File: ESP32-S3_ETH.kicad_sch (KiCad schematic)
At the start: 14 parts, among them J1 Screw_Terminal_01x02, J2 Screw_Terminal_01x04, J3 SSW-104-01-F-S, J4 SSW-108-02-G-D, J5 Screw_Terminal_01x03, J6 Screw_Terminal_01x03, U1 ESP32-S3-ETH

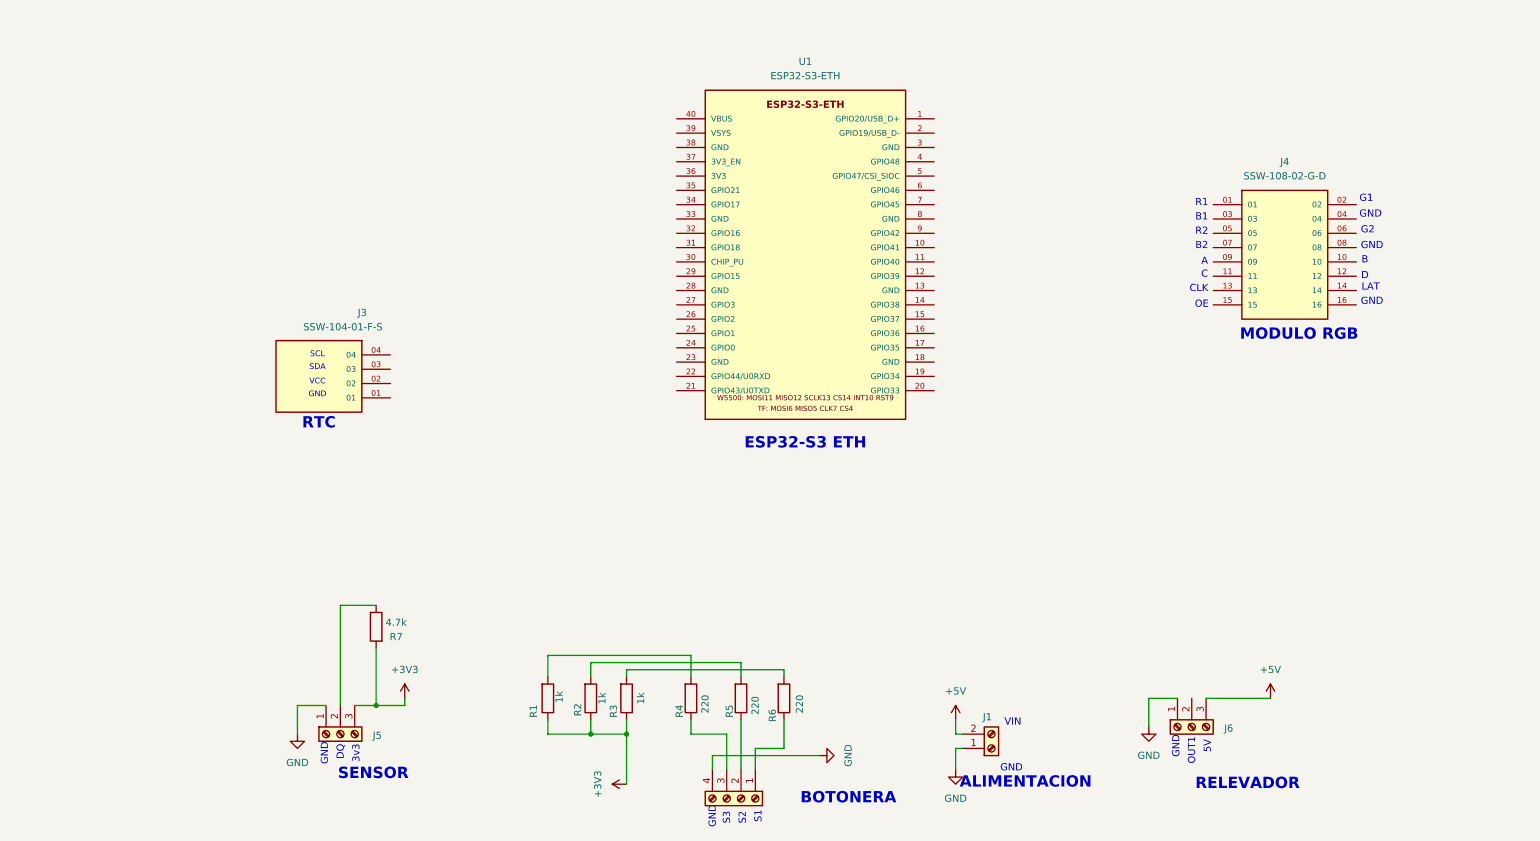
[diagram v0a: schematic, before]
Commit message: ssw-120-1 added
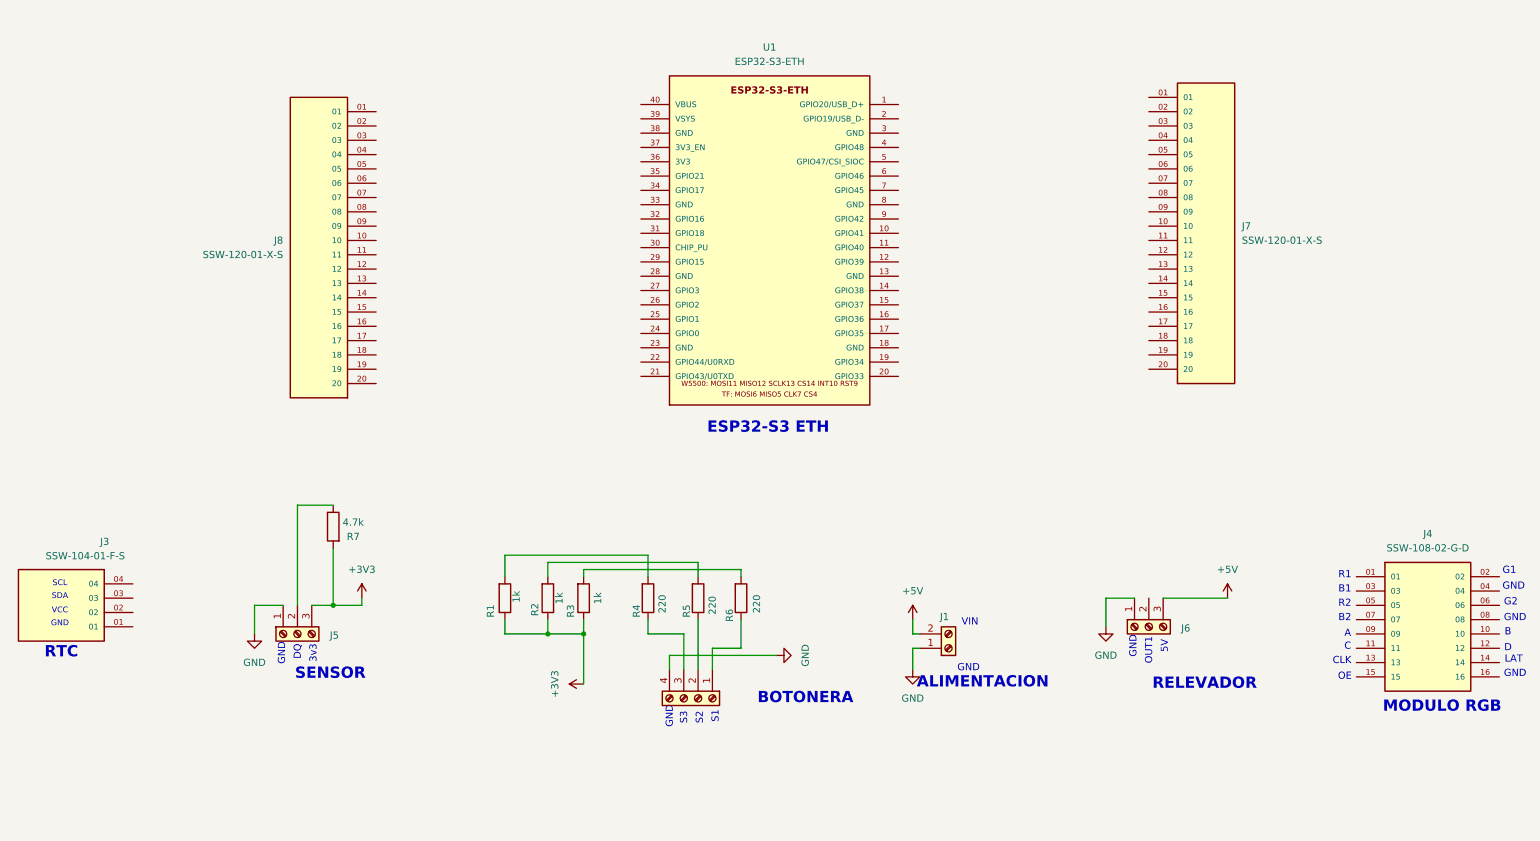
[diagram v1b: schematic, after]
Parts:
- added J7, J8: SSW-120-01-X-S, symbol SSW-120-01-X-S:SSW-120-01-X-S
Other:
- moved on the sheet: J1, J3, J4, J5, J6, R1, R2, R3, R4, R5, R6, R7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

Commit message: Ground plane and power size trace in process
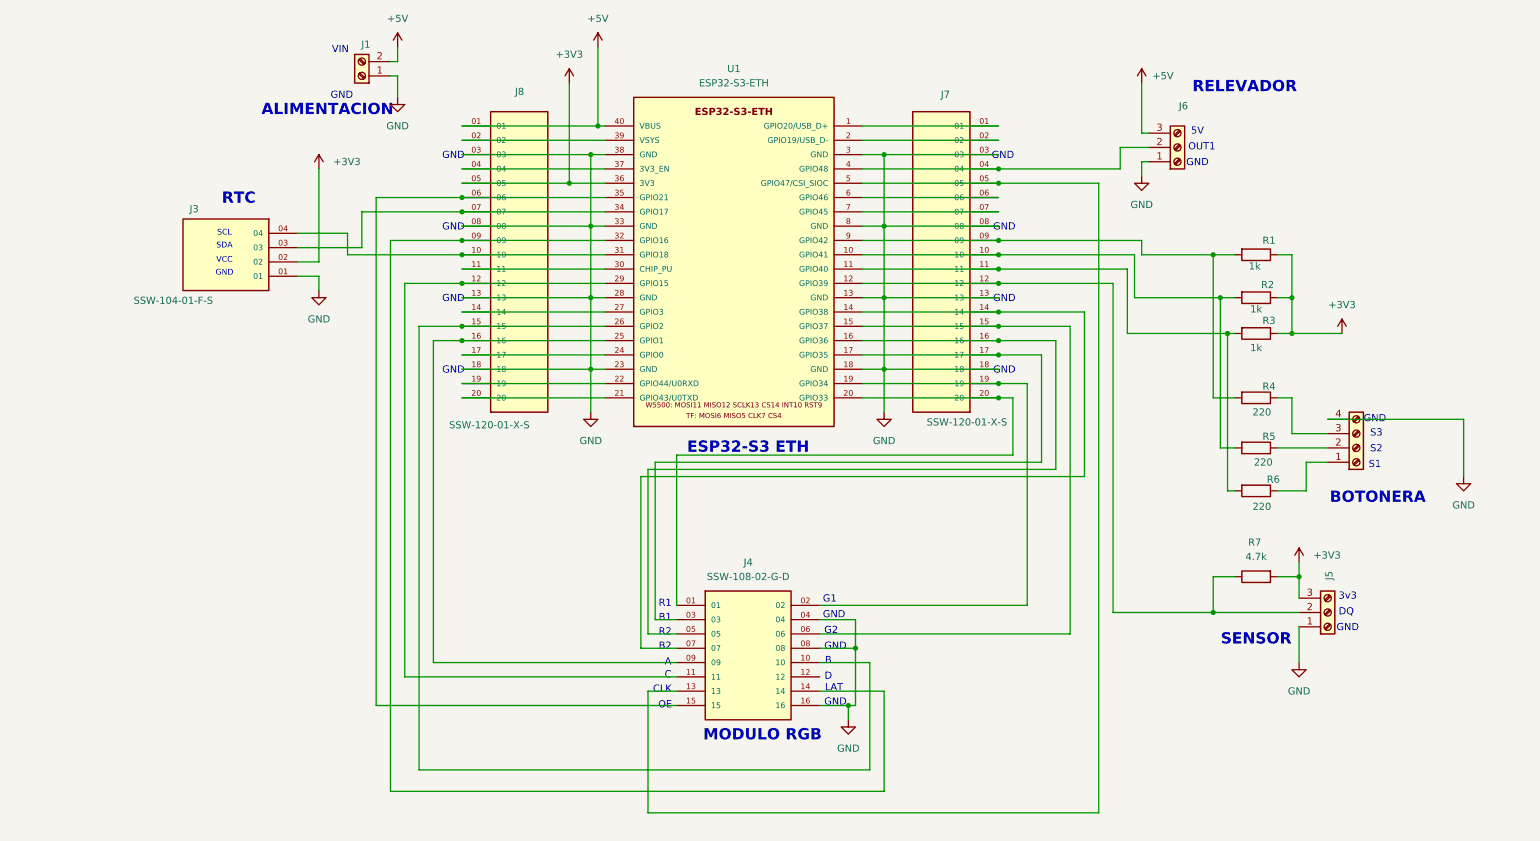
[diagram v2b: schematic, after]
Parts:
- J7, J8: footprint (none) -> SSW-120-01-X-S:SAMTEC_SSW-120-01-X-S
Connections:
- net +3V3: now also J3.02, J8.05, U1.36 (3V3)
- net +5V: now also J8.01, U1.40 (VBUS)
- net GND: now also J3.01, J4.04, J4.08, J4.16, J7.03, J7.08, J7.13, J7.18, J8.03, J8.08, J8.13, J8.18, U1.13 (GND), U1.18 (GND), U1.23 (GND), U1.28 (GND), U1.3 (GND), U1.33 (GND), U1.38 (GND), U1.8 (GND)
- net at R1.2, R4.2: now also J7.09, U1.9 (GPIO42)
- net at R2.2, R5.2: now also J7.10, U1.10 (GPIO41)
- net at U1.1 (GPIO20/USB_D+): now also J7.01
- net at U1.11 (GPIO40): now also J7.11, R3.2, R6.2
- net at U1.12 (GPIO39): now also J5.2 (Pin_2), J7.12, R7.1
- net at U1.14 (GPIO38): now also J4.07, J7.14
- net at U1.15 (GPIO37): now also J4.06, J7.15
- net at U1.16 (GPIO36): now also J4.05, J7.16
- net at U1.17 (GPIO35): now also J4.03, J7.17
- net at U1.19 (GPIO34): now also J4.02, J7.19
- net at U1.2 (GPIO19/USB_D-): now also J7.02
- net at U1.20 (GPIO33): now also J4.01, J7.20
- net at U1.21 (GPIO43/U0TXD): now also J8.20
- net at U1.22 (GPIO44/U0RXD): now also J8.19
- net at U1.24 (GPIO0): now also J8.17
- net at U1.25 (GPIO1): now also J4.09, J8.16
- net at U1.26 (GPIO2): now also J4.10, J8.15
- net at U1.27 (GPIO3): now also J8.14
- net at U1.29 (GPIO15): now also J4.11, J8.12
- net at U1.30 (CHIP_PU): now also J8.11
- net at U1.31 (GPIO18): now also J3.04, J8.10
- net at U1.32 (GPIO16): now also J4.14, J8.09
- net at U1.34 (GPIO17): now also J3.03, J8.07
- net at U1.35 (GPIO21): now also J4.15, J8.06
- net at U1.37 (3V3_EN): now also J8.04
- net at U1.39 (VSYS): now also J8.02
- net at U1.4 (GPIO48): now also J6.2 (Pin_2), J7.04
- net at U1.5 (GPIO47/CSI_SIOC): now also J4.13, J7.05
- net at U1.6 (GPIO46): now also J7.06
- net at U1.7 (GPIO45): now also J7.07
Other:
- moved on the sheet: J1, J3, J4, J5, J6, J7, J8, R1, R2, R3, R4, R5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
